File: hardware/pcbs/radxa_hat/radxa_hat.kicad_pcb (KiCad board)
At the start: 2 copper layers, 65 x 26.5 mm, 10 parts, among them J1 RADXA_HEADER, J2 Header_01x06, J3 Header_01x04, J4 Header_01x08, J5 Header_01x04

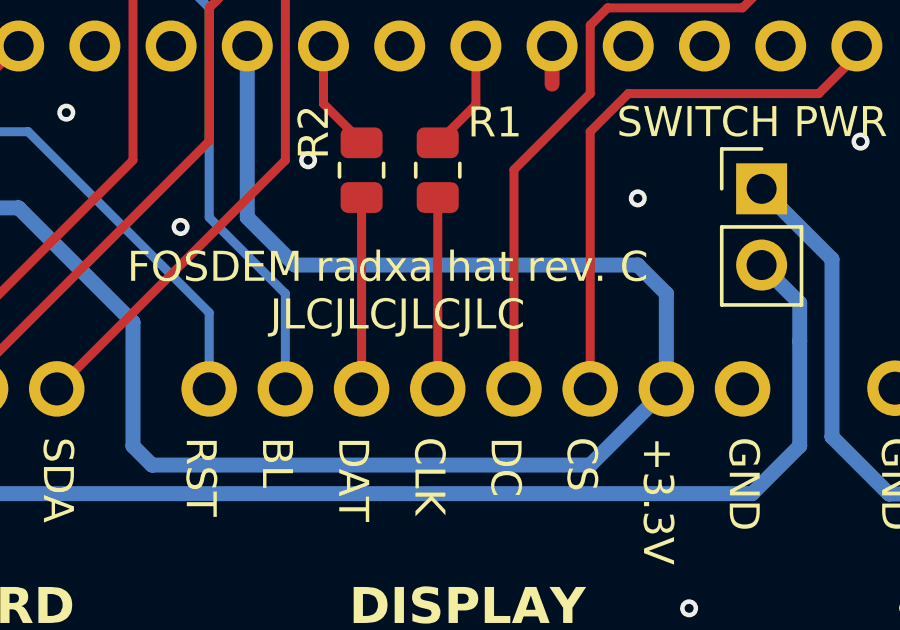
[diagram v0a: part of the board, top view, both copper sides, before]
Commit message: boards: fix minor mistakes and aisler IDs
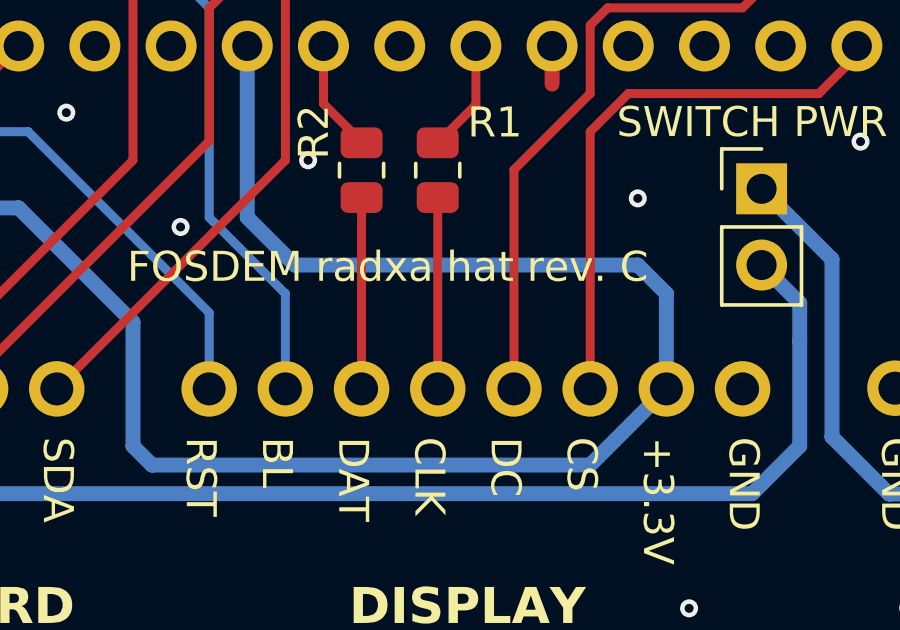
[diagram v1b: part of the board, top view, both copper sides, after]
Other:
- board text removed: "JLCJLCJLCJLC"
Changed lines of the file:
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@@
-		)
-	)
-	(gr_text "JLCJLCJLCJLC"
-		(at 153.67 102.235 0)
-		(layer "F.SilkS")
-		(effects
-			(font
-				(size 1 1)
-				(thickness 0.1)
-			)
-			(justify left bottom)
 		)
 	)

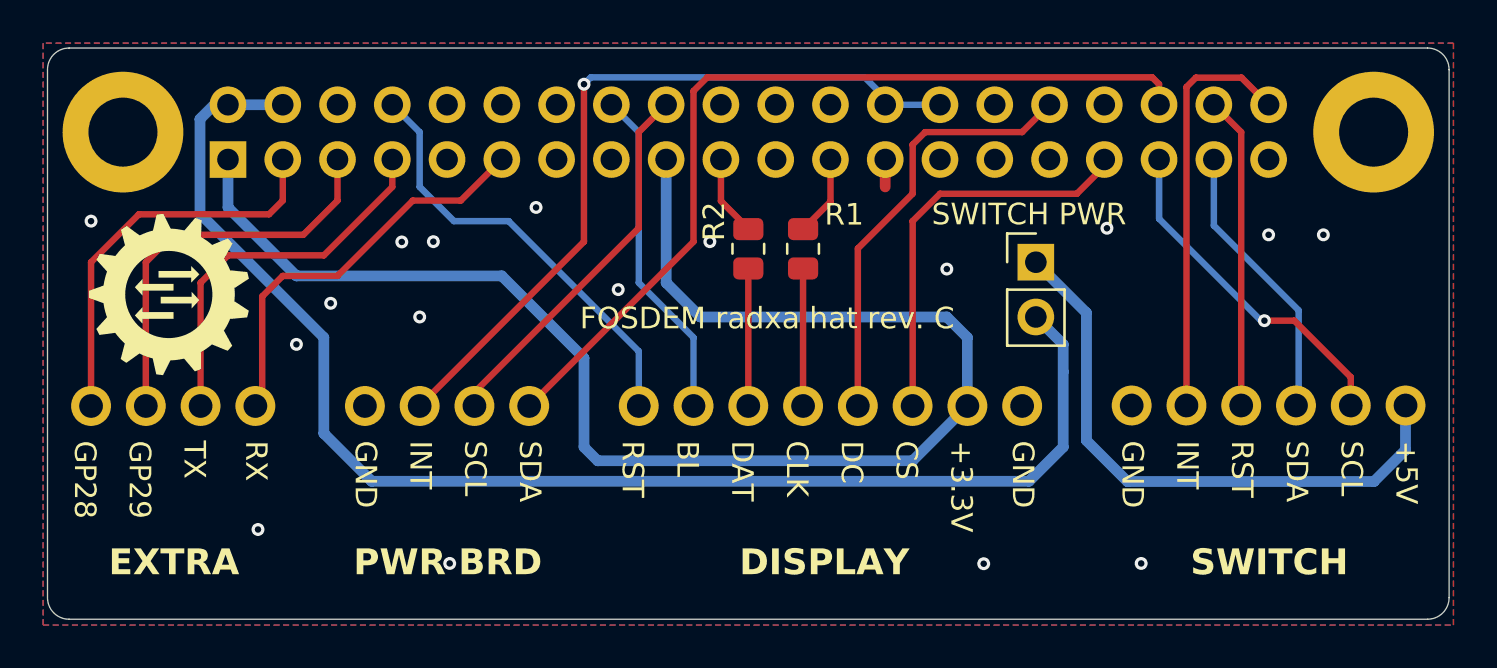
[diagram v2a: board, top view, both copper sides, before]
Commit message: hat_pcbs: more space under MTA100 connectors as per datasheet
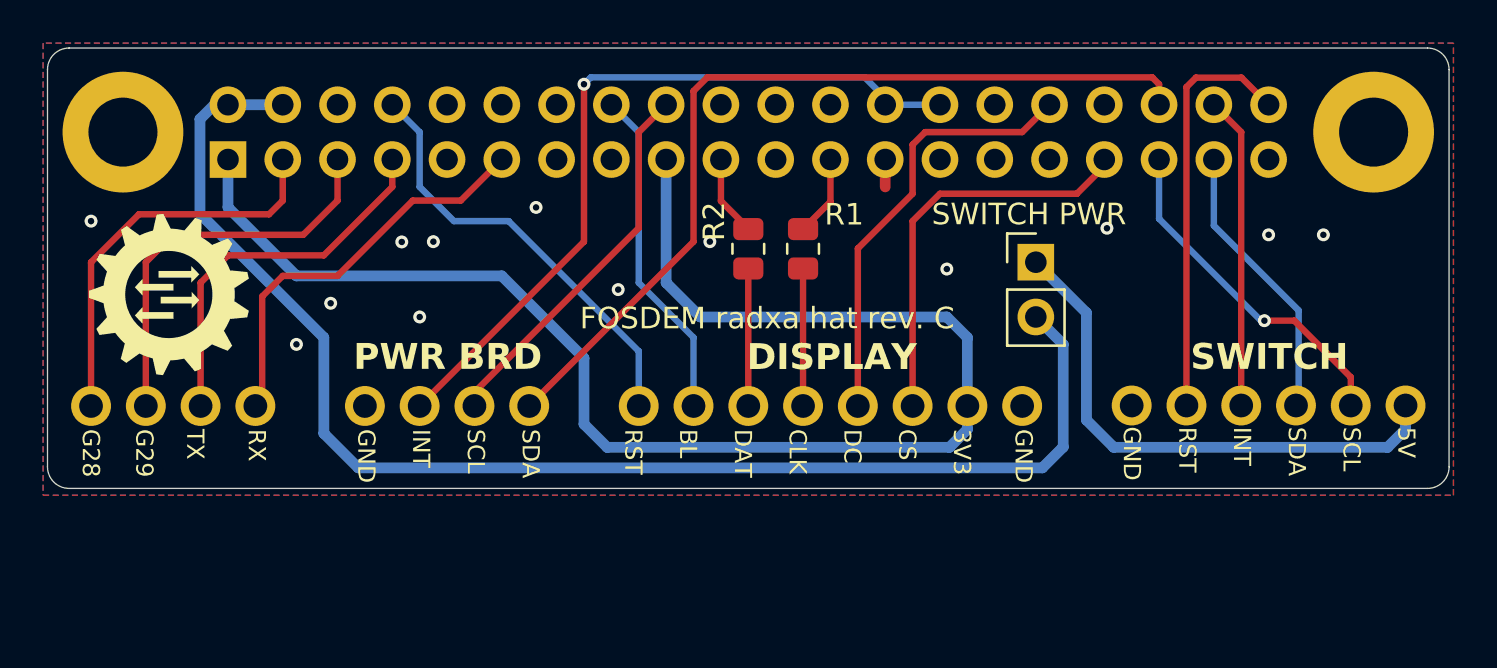
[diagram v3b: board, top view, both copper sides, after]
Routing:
- net Net-(J2-Pin_6): track 27.5 -> 25.1 mm
- net +5V: track 63.5 -> 63.0 mm
- net +3.3V: track 68.8 -> 68.3 mm
- net GND: vias 17 -> 13
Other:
- board size 65 x 26.5 mm -> 65 x 20.4 mm
- board text added: "3V3"
- board text added: "5V"
- board text added: "G28"
- board text added: "G29"
- board text removed: "+3.3V"
- board text removed: "+5V"
- board text removed: "EXTRA"
- board text removed: "GP28"
- board text removed: "GP29"
